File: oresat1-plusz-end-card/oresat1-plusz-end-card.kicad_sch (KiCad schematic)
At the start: 38 parts, among them J1 J-SAMTEC-TFM-120-01-L-D-RA, J2 M55-7101242R, J3 M55-7101242R, J4 M55-7101242R, J5 M55-7101242R, J6 U.FL-R-SMT-1

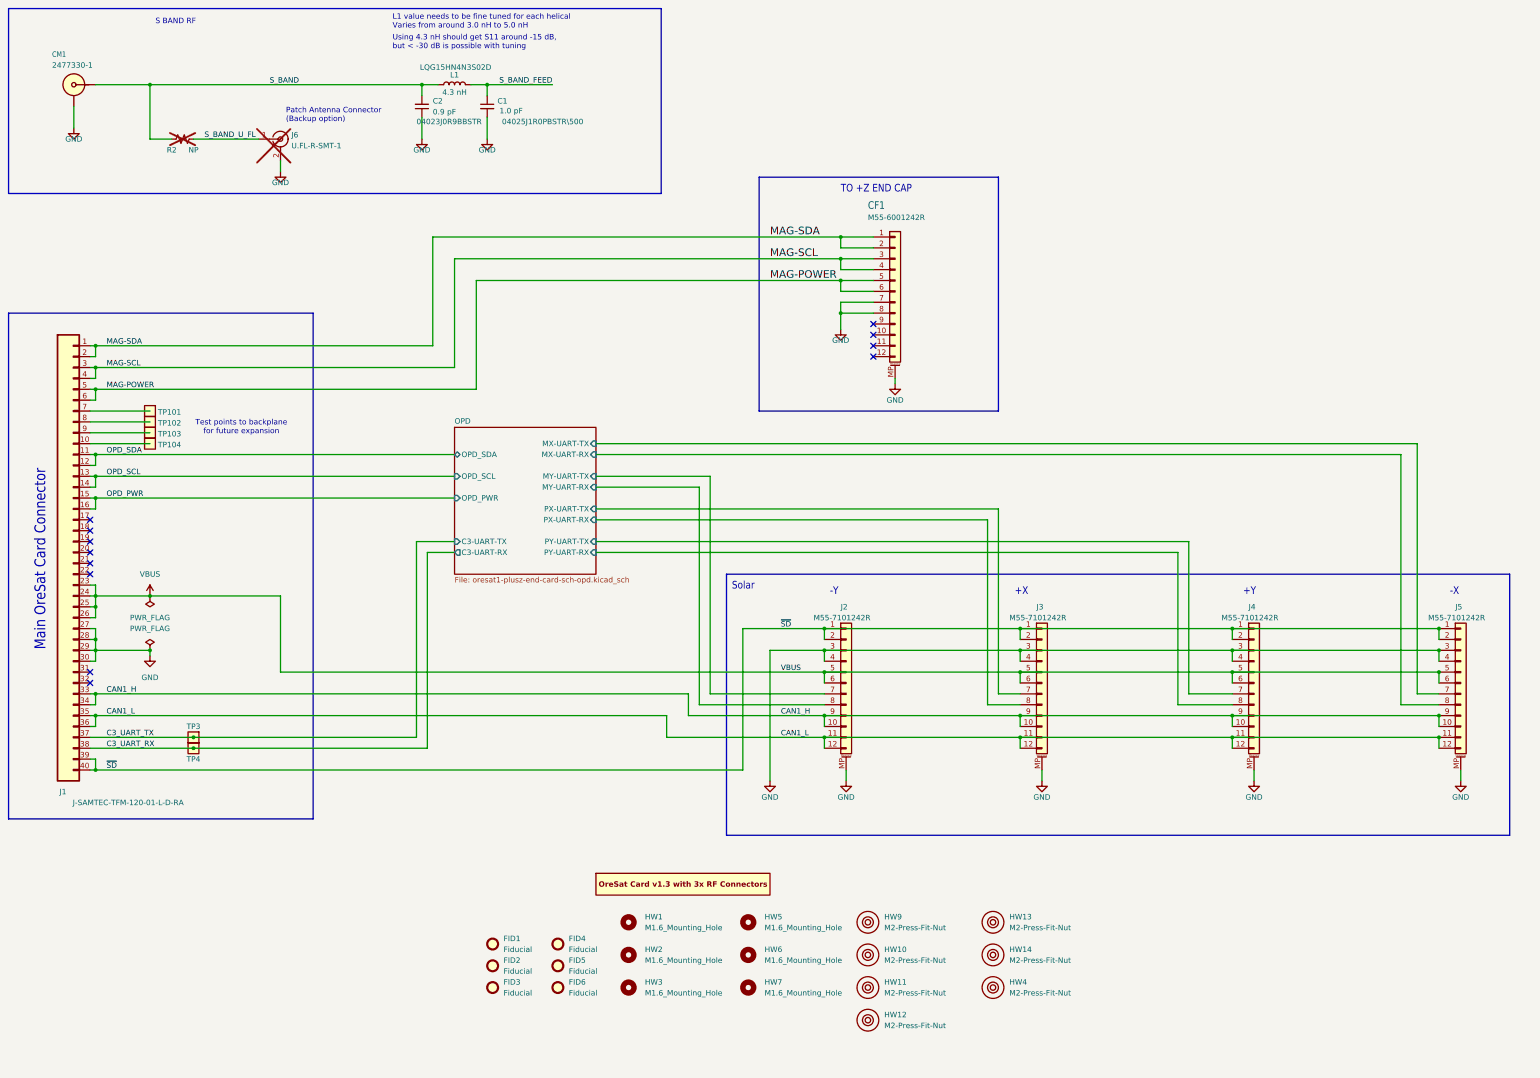
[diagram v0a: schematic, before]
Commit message: Fixed OPD connection in schematics and updated tracing and out of date footprints. Ready for final review from andrew
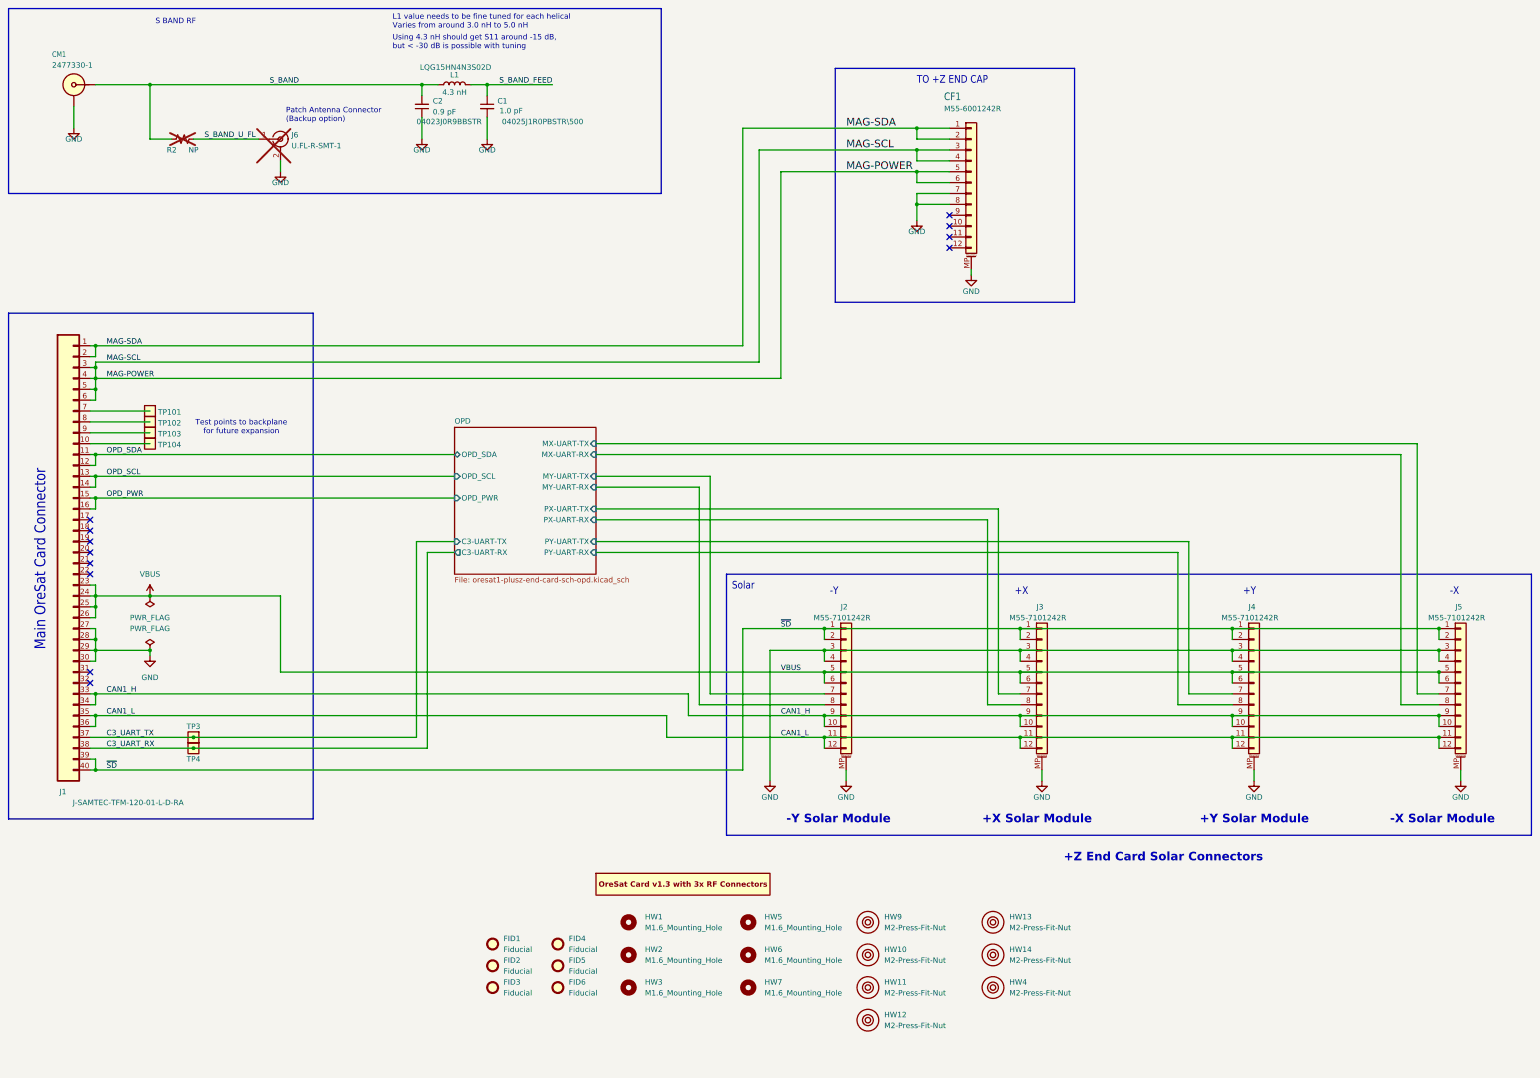
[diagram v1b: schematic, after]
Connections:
- net MAG-SCL is gone; now on net MAG-POWER: CF1.3 (Pin_3), CF1.4 (Pin_4), J1.3, J1.4
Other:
- note added: "+X Solar Module"
- note added: "+Y Solar Module"
- note added: "+Z End Card Solar Connectors"
- note added: "-X Solar Module"
- note added: "-Y Solar Module"
- moved on the sheet: CF1

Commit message: added clearance around HW
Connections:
- net MAG-POWER: no longer CF1.3 (Pin_3), CF1.4 (Pin_4), J1.3, J1.4
- new net MAG-SCL: CF1.3 (Pin_3), CF1.4 (Pin_4), J1.3, J1.4
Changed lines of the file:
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@@
-	)
-	(junction
-		(at 68.58 104.14)
-		(diameter 0)
-		(color 0 0 0 0)
 	)
 	(junction
@@
 	(wire
 		(pts
-			(xy 68.58 100.33) (xy 68.58 101.6)
-		)
-		(stroke
-			(width 0)
-			(type default)
-		)
-	)
-	(wire
-		(pts
 			(xy 238.76 182.88) (xy 284.48 182.88)
 		)
@@
 	(wire
 		(pts
-			(xy 68.58 104.14) (xy 68.58 106.68)
-		)
-		(stroke
-			(width 0)
-			(type default)
-		)
-	)
-	(wire
-		(pts
 			(xy 284.48 182.88) (xy 334.01 182.88)
 		)
@@
 	(wire
 		(pts
-			(xy 223.52 50.8) (xy 223.52 100.33)
+			(xy 223.52 50.8) (xy 223.52 101.6)
 		)
 		(stroke
@@
 	(wire
 		(pts
-			(xy 228.6 104.14) (xy 228.6 55.88)
+			(xy 228.6 106.68) (xy 228.6 55.88)
 		)
 		(stroke
@@
 	(wire
 		(pts
-			(xy 68.58 100.33) (xy 223.52 100.33)
+			(xy 68.58 101.6) (xy 223.52 101.6)
 		)
 		(stroke
@@
 	(wire
 		(pts
-			(xy 68.58 104.14) (xy 228.6 104.14)
+			(xy 68.58 106.68) (xy 228.6 106.68)
 		)
 		(stroke
@@
 	)
 	(label "MAG-POWER"
-		(at 71.12 104.14 0)
+		(at 71.12 106.68 0)
 		(effects
 			(font
@@
 	)
 	(label "MAG-SCL"
-		(at 71.12 100.33 0)
+		(at 71.12 101.6 0)
 		(effects
 			(font

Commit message: SBAND & HELICAL RF CHANGES
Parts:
- removed R2: NP, Resistor_SMD:R_0402_1005Metric, symbol Device:R_Small_US
- added CM2: 2477330-1, oresat-connectors:J-MOLEX-SMPM-073300-002X, symbol oresat-connectors:J-MOLEX-SMPM-73300-002X
- J6: now fitted
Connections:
- net GND: now also CM2.SHLD
- net S_BAND: no longer names the net of C2.2, CM1.SIG, L1.1
- net S_BAND_FEED renamed HELICAL
- net S_BAND_U_FL renamed PATCH
- net PATCH: now also CM2.SIG
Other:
- note added: "HELCIAL"
- note added: "PATCH"
- note removed: "S BAND RF"

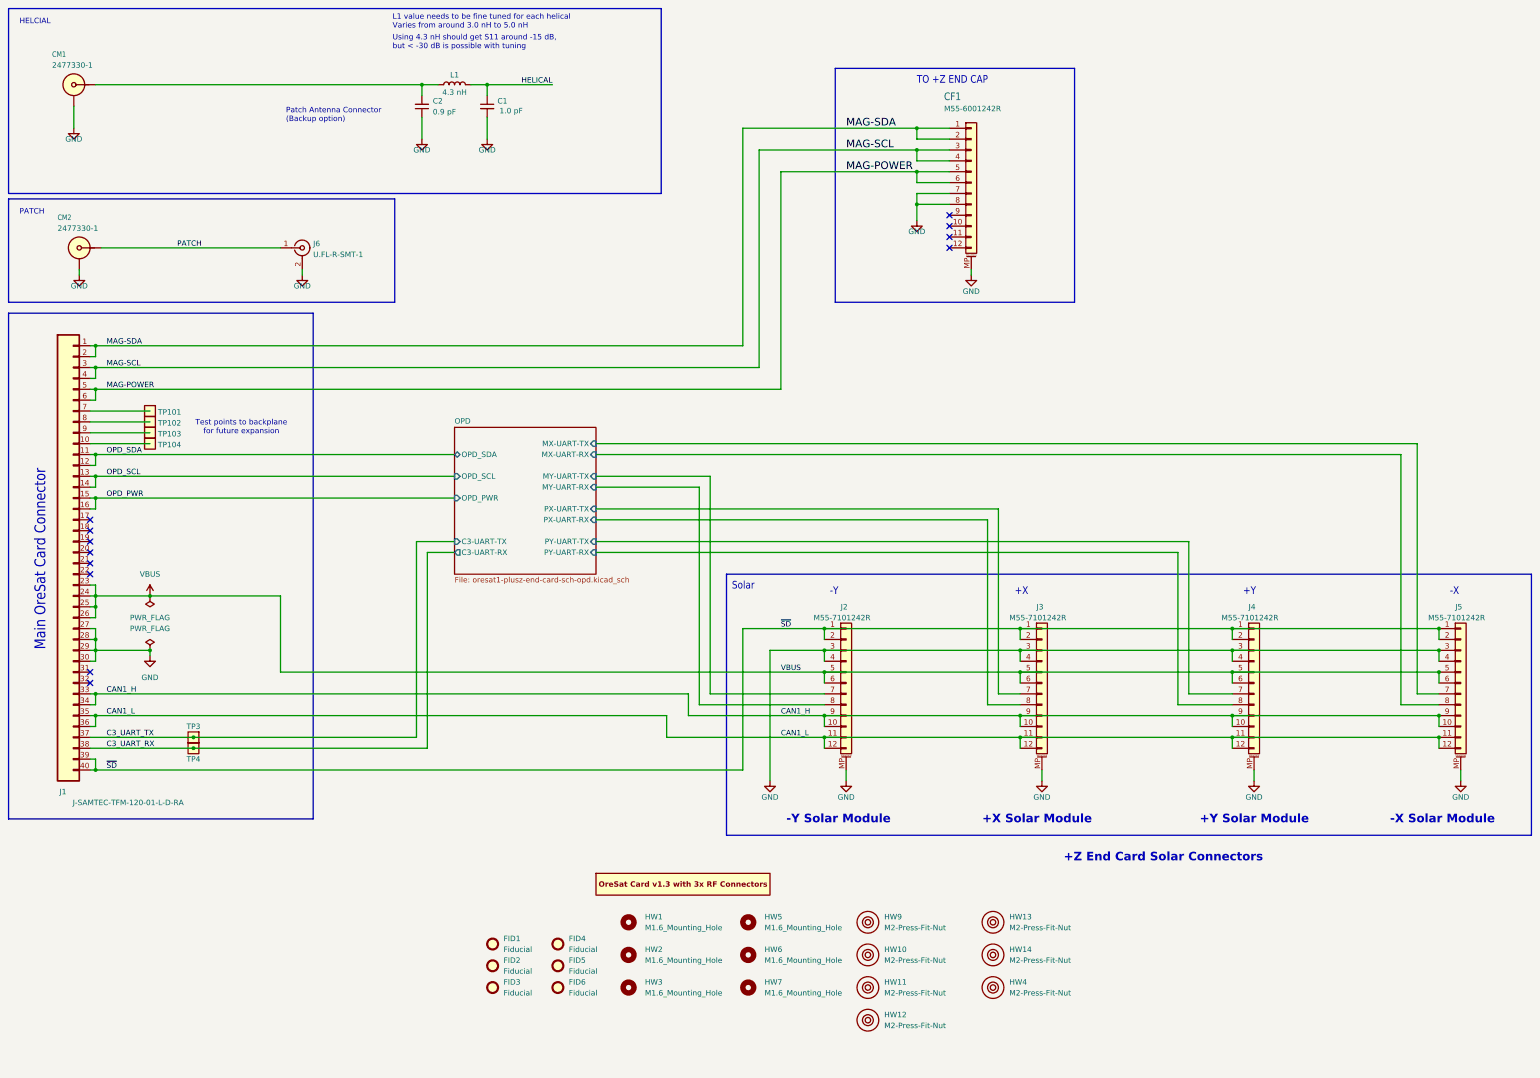
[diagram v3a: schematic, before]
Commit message: Another round on the +Z End Card; ready for fab.
Brushed up RF paths and solder mask, cleaned up UART switches with closer bypass caps, cleaned up a lot of the zones, and lots of little polishing.
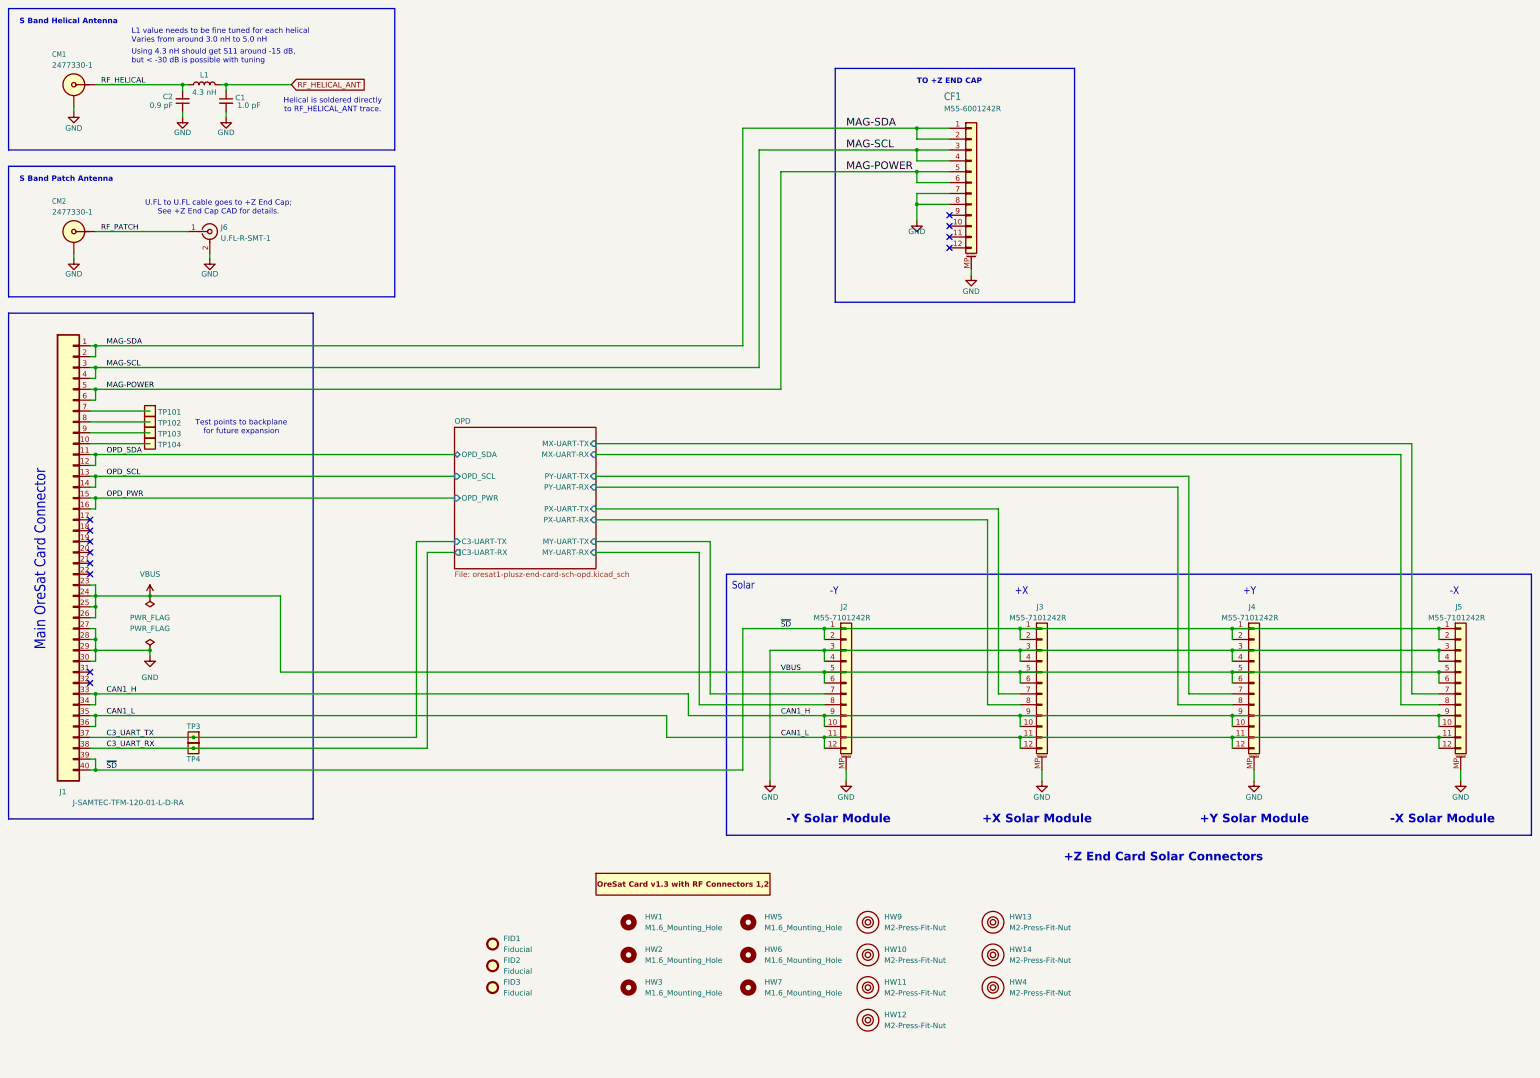
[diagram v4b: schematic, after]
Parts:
- removed FID4, FID5, FID6: Fiducial, Fiducial:Fiducial_1mm_Mask2mm, symbol Mechanical:Fiducial
- J1: MFR Samtec -> Samtec Inc.
- PCB1: footprint oresat-pcbs:ORESAT-CARD-V1.3-3RF -> oresat-pcbs:ORESAT-CARD-V1.3-2RF-LEFT; symbol oresat-pcbs:ORESAT-CARD-V1.3-3RF -> oresat-pcbs:ORESAT-CARD-V1.3-2RF-LEFT; now in the parts list
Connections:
- net RF_HELICAL: now reaches C2.2, CM1.SIG, L1.1
- net HELICAL renamed RF_HELICAL_ANT
- net PATCH renamed RF_PATCH
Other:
- note added: "Helical is soldered directly to RF_HELICAL_ANT trace."
- note added: "S Band Helical Antenna"
- note added: "S Band Patch Antenna"
- note added: "U.FL to U.FL cable goes to +Z End Cap; See +Z End Cap CAD for details."
- note removed: "HELCIAL"
- note removed: "PATCH"
- note removed: "Patch Antenna Connector (Backup option)"
- moved on the sheet: C1, C2, CM2, J6, L1

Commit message: v1.1 sent to fab
Updated 3D models of connectors, added missing capacitors, fixed footprints, polished schematic, upgraded to single README file with Makefile.
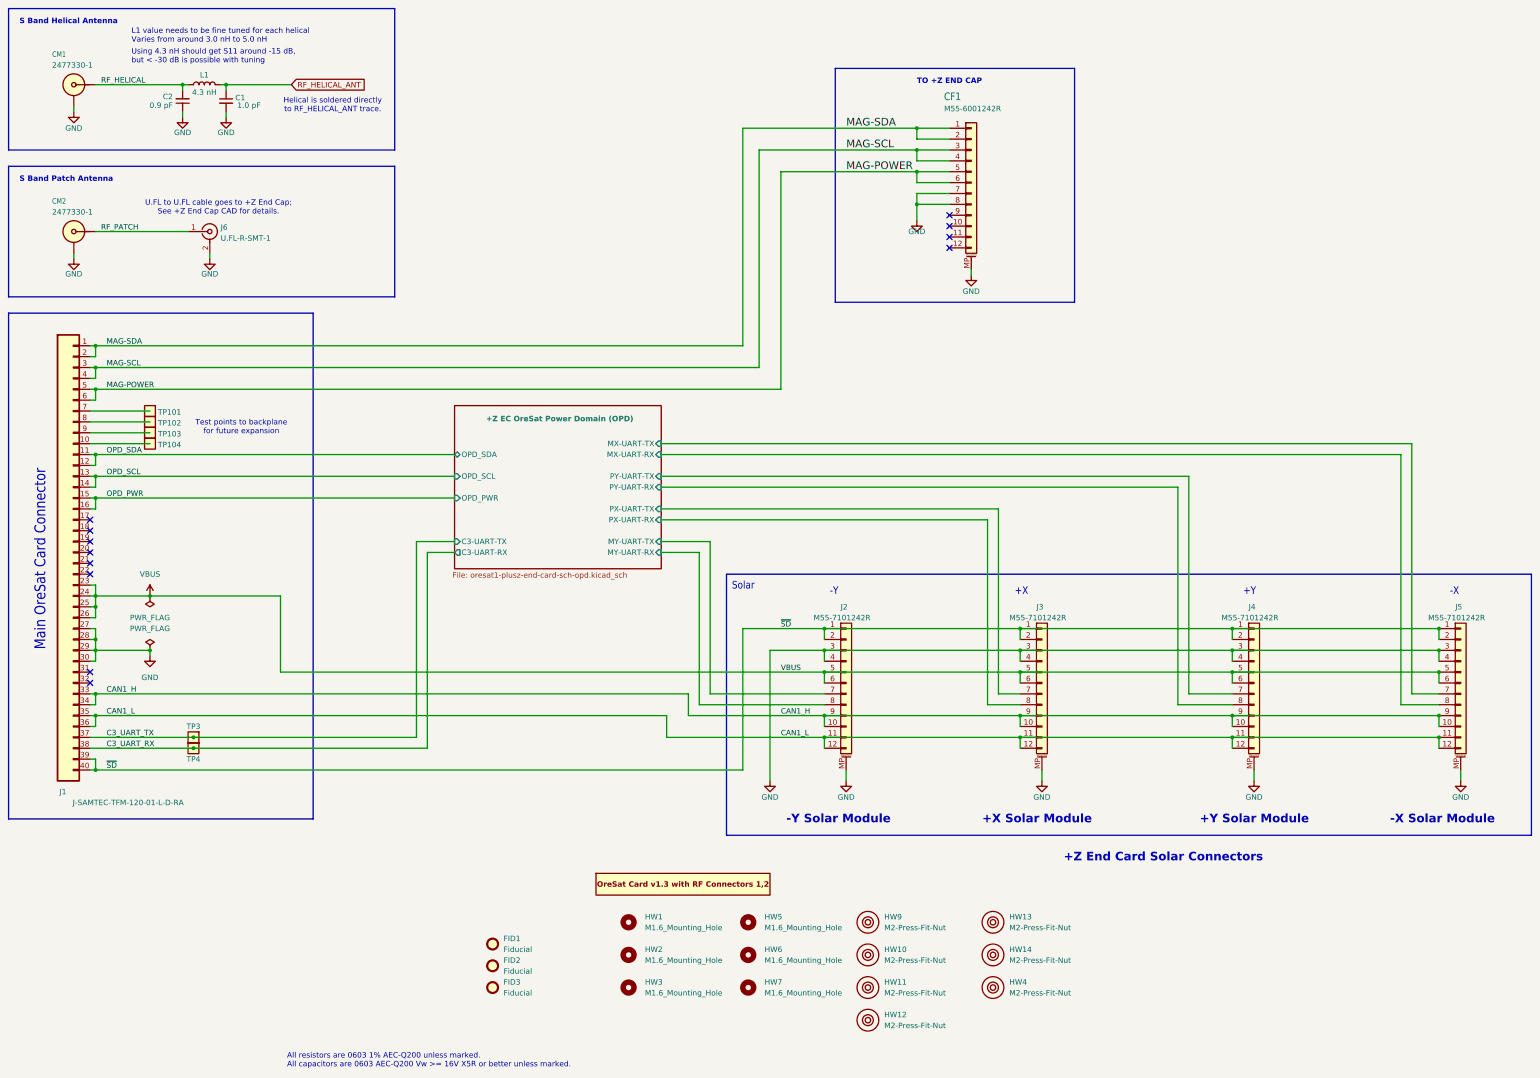
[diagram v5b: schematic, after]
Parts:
- HW10, HW11, HW12, HW13, HW14, HW4, HW9: DIS (none) -> McMaster-Carr; DPN (none) -> 94100A150; MFR (none) -> N/A; MPN (none) -> N/A; now in the parts list
- PCB1: DIS (none) -> N/A; DPN (none) -> N/A; MFR (none) -> N/A; MPN (none) -> N/A
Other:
- sheet OPD renamed +Z EC OreSat Power Domain (OPD)
- note added: "All resistors are 0603 1% AEC-Q200 unless marked. All capacitors are 0603 AEC-Q200 Vw >= 16V X5R or better unless marked."
